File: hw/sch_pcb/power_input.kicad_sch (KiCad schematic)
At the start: 22 parts, among them J2 WAGO 256 RED, J3 WAGO 256 BLUE, J4 HEADER_2x01_PARALLEL, U3 SPV1040

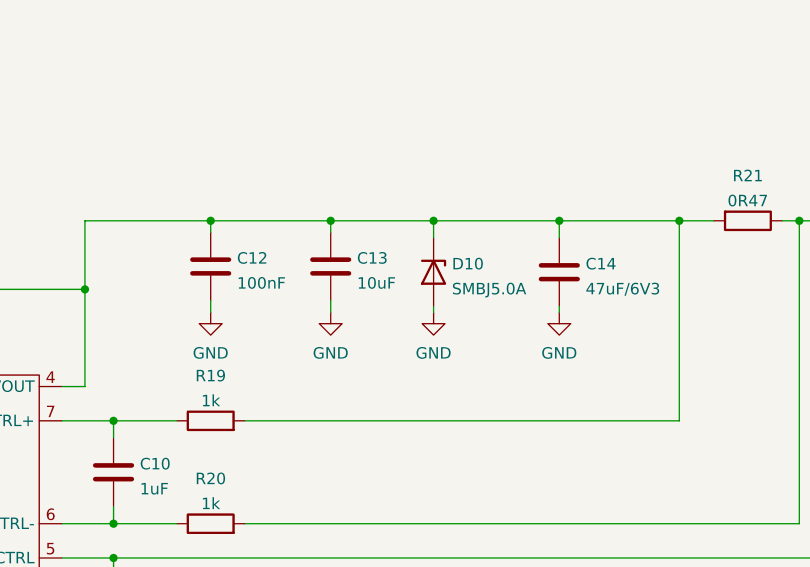
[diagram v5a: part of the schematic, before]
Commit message: Edit UST ID
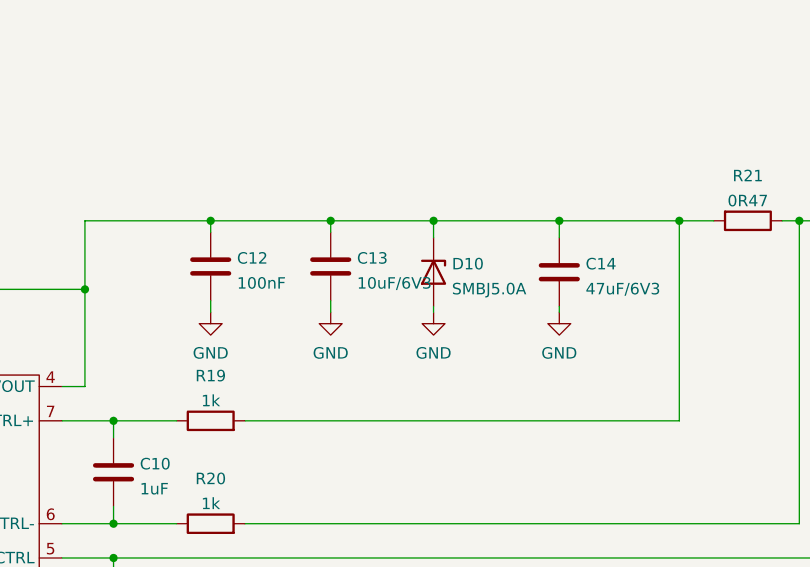
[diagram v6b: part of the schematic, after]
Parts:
- C10: UST_ID (none) -> 5c70984712875079b91f8b50
- C11: UST_ID (none) -> 5c70984712875079b91f8b45
- C12, C9: UST_ID (none) -> 5c70984712875079b91f8b4c
- C13: value 10uF -> 10uF/6V3; UST_ID (none) -> 5c70984712875079b91f8b53
- C14, C15, C8: UST_ID (none) -> 60d580ff1287500165f8595a
- D10: UST_ID (none) -> 5c70984512875079b91f88c7
- D9: UST_ID (none) -> 5c70984512875079b91f88b0
- J2: value WAGO 256 RED -> WAGO 256 ORANGE; UST_ID (none) -> 5c70984412875079b91f87c4
- J3: UST_ID (none) -> 5c70984412875079b91f87c3
- L1: UST_ID (none) -> 5c70984412875079b91f8822
- R17, R18, R19, R20: UST_ID (none) -> 5c70984512875079b91f898c
- R21: UST_ID (none) -> 60be2ed51287500165e6c1cd
- R22: UST_ID (none) -> 5c70984712875079b91f8aa6
- R23: UST_ID (none) -> 5c70984712875079b91f8aa0
- U3: UST_ID (none) -> 5c70984612875079b91f89bc
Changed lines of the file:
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@@
       (effects (font (size 1.27 1.27)) hide)
     )
-    (property "UST_ID" "" (id 4) (at 141.605 106.68 0)
+    (property "UST_ID" "5c70984712875079b91f8b45" (id 4) (at 141.605 106.68 0)
       (effects (font (size 1.27 1.27)) hide)
     )
@@
       (effects (font (size 1.27 1.27)) hide)
     )
-    (property "UST_ID" "" (id 4) (at 93.345 106.68 0)
+    (property "UST_ID" "5c70984712875079b91f8b4c" (id 4) (at 93.345 106.68 0)
       (effects (font (size 1.27 1.27)) hide)
     )
@@
       (effects (font (size 1.27 1.27)) hide)
     )
-    (property "UST_ID" "" (id 4) (at 152.4 68.58 0)
+    (property "UST_ID" "5c70984712875079b91f8b4c" (id 4) (at 152.4 68.58 0)
       (effects (font (size 1.27 1.27)) hide)
     )
@@
       (effects (font (size 1.27 1.27)) (justify left))
     )
-    (property "Value" "10uF" (id 1) (at 168.656 70.4466 0)
+    (property "Value" "10uF/6V3" (id 1) (at 168.656 70.4466 0)
       (effects (font (size 1.27 1.27)) (justify left))
     )
@@
       (effects (font (size 1.27 1.27)) hide)
     )
-    (property "UST_ID" "" (id 4) (at 165.735 68.58 0)
+    (property "UST_ID" "5c70984712875079b91f8b53" (id 4) (at 165.735 68.58 0)
       (effects (font (size 1.27 1.27)) hide)
     )
@@
       (effects (font (size 1.27 1.27)) hide)
     )
-    (property "UST_ID" "" (id 4) (at 222.885 105.41 0)
+    (property "UST_ID" "5c70984712875079b91f8aa0" (id 4) (at 222.885 105.41 0)
       (effects (font (size 1.27 1.27)) hide)
     )
@@
       (effects (font (size 1.27 1.27)) hide)
     )
-    (property "UST_ID" "" (id 4) (at 177.165 69.215 0)
+    (property "UST_ID" "5c70984512875079b91f88c7" (id 4) (at 177.165 69.215 0)
       (effects (font (size 1.27 1.27)) hide)
     )
@@
       (effects (font (size 1.27 1.27)) hide)
     )
-    (property "UST_ID" "" (id 4) (at 123.19 88.265 0)
+    (property "UST_ID" "5c70984612875079b91f89bc" (id 4) (at 123.19 88.265 0)
       (effects (font (size 1.27 1.27)) hide)
     )
@@
       (effects (font (size 1.27 1.27)) hide)
     )
+    (property "UST_ID" "60d580ff1287500165f8595a" (id 4) (at 191.135 69.215 0)
+      (effects (font (size 1.27 1.27)) hide)
+    )
     (pin "1")
     (pin "2")
@@
     )
     (property "Datasheet" "~" (id 3) (at 67.945 95.885 0)
+      (effects (font (size 1.27 1.27)) hide)
+    )
+    (property "UST_ID" "60d580ff1287500165f8595a" (id 4) (at 67.945 95.885 0)
       (effects (font (size 1.27 1.27)) hide)
     )
@@
       (effects (font (size 1.27 1.27)) hide)
     )
-    (property "UST_ID" "" (id 4) (at 122.555 71.12 0)
+    (property "UST_ID" "5c70984512875079b91f88b0" (id 4) (at 122.555 71.12 0)
       (effects (font (size 1.27 1.27)) hide)
     )
@@
       (effects (font (size 1.524 1.524)))
     )
-    (property "UST_ID" "" (id 4) (at 53.34 102.235 0)
+    (property "UST_ID" "5c70984412875079b91f87c3" (id 4) (at 53.34 102.235 0)
       (effects (font (size 1.27 1.27)) hide)
     )
@@
     (in_bom yes) (on_board yes)
     (property "Reference" "J2" (id 0) (at 52.705 81.915 0))
-    (property "Value" "WAGO 256 RED" (id 1) (at 50.8 79.375 0)
+    (property "Value" "WAGO 256 ORANGE" (id 1) (at 50.8 79.375 0)
       (effects (font (size 1.016 1.016)) hide)
     )
@@
       (effects (font (size 1.524 1.524)))
     )
-    (property "UST_ID" "" (id 4) (at 53.34 80.645 0)
+    (property "UST_ID" "5c70984412875079b91f87c4" (id 4) (at 53.34 80.645 0)
       (effects (font (size 1.27 1.27)) hide)
     )
@@
       (effects (font (size 1.27 1.27)) hide)
     )
-    (property "UST_ID" "" (id 4) (at 152.4 97.155 0)
+    (property "UST_ID" "5c70984512875079b91f898c" (id 4) (at 152.4 97.155 0)
       (effects (font (size 1.27 1.27)) hide)
     )
@@
       (effects (font (size 1.27 1.27)) hide)
     )
-    (property "UST_ID" "" (id 4) (at 82.55 94.615 0)
+    (property "UST_ID" "5c70984512875079b91f898c" (id 4) (at 82.55 94.615 0)
       (effects (font (size 1.27 1.27)) hide)
     )
@@
       (effects (font (size 1.27 1.27)) hide)
     )
-    (property "UST_ID" "" (id 4) (at 95.885 88.265 0)
+    (property "UST_ID" "5c70984512875079b91f898c" (id 4) (at 95.885 88.265 0)
       (effects (font (size 1.27 1.27)) hide)
     )
@@
     )
     (property "Datasheet" "~" (id 3) (at 229.87 69.215 0)
+      (effects (font (size 1.27 1.27)) hide)
+    )
+    (property "UST_ID" "60d580ff1287500165f8595a" (id 4) (at 229.87 69.215 0)
       (effects (font (size 1.27 1.27)) hide)
     )
@@
       (effects (font (size 1.27 1.27)) hide)
     )
-    (property "UST_ID" "" (id 4) (at 152.4 85.725 0)
+    (property "UST_ID" "5c70984512875079b91f898c" (id 4) (at 152.4 85.725 0)
       (effects (font (size 1.27 1.27)) hide)
     )
@@
       (effects (font (size 1.27 1.27)) hide)
     )
-    (property "UST_ID" "" (id 4) (at 212.09 63.5 0)
+    (property "UST_ID" "60be2ed51287500165e6c1cd" (id 4) (at 212.09 63.5 0)
       (effects (font (size 1.27 1.27)) hide)
     )
@@
       (effects (font (size 1.27 1.27)) hide)
     )
-    (property "UST_ID" "" (id 4) (at 141.605 91.44 0)
+    (property "UST_ID" "5c70984712875079b91f8b50" (id 4) (at 141.605 91.44 0)
       (effects (font (size 1.27 1.27)) hide)
     )
@@
       (effects (font (size 1.27 1.27)) hide)
     )
-    (property "UST_ID" "" (id 4) (at 222.885 93.345 0)
+    (property "UST_ID" "5c70984712875079b91f8aa6" (id 4) (at 222.885 93.345 0)
       (effects (font (size 1.27 1.27)) hide)
     )
@@
       (effects (font (size 1.27 1.27)) hide)
     )
-    (property "UST_ID" "" (id 4) (at 102.87 81.915 0)
-      (effects (font (size 1.27 1.27)) hide)
-    )
+    (property "UST_ID" "5c70984412875079b91f8822" (id 4) (at 102.87 81.915 0)
+      (effects (font (size 1.27 1.27)) hide)
+    )

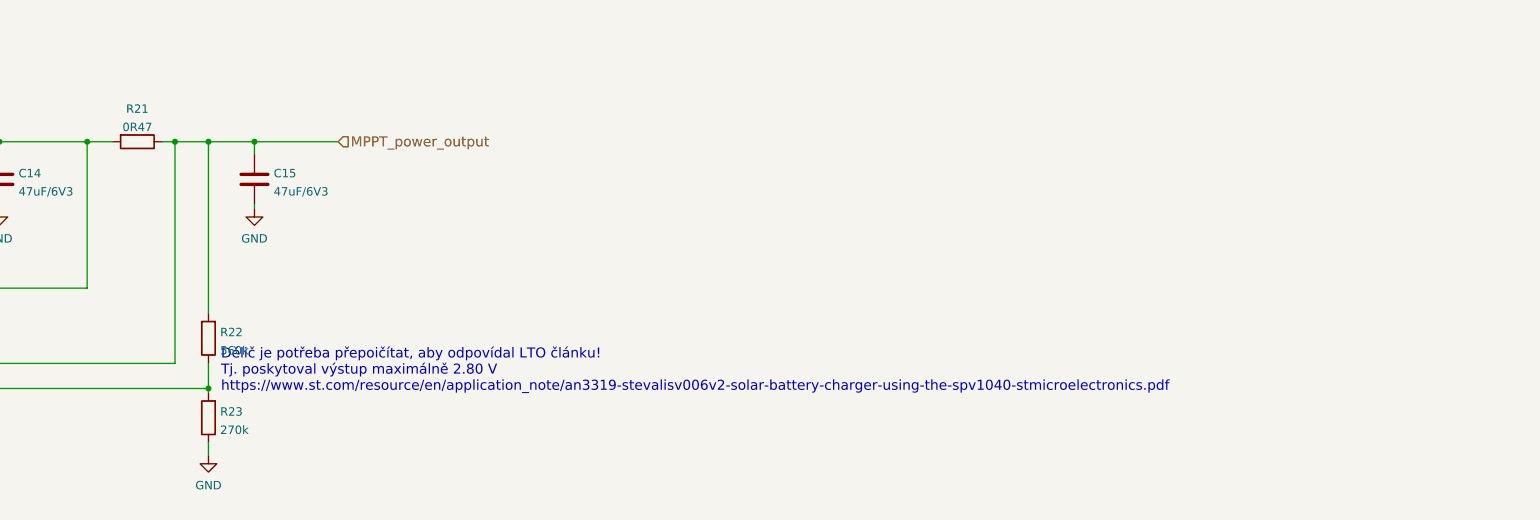
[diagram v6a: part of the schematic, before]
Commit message: Edit UST ID
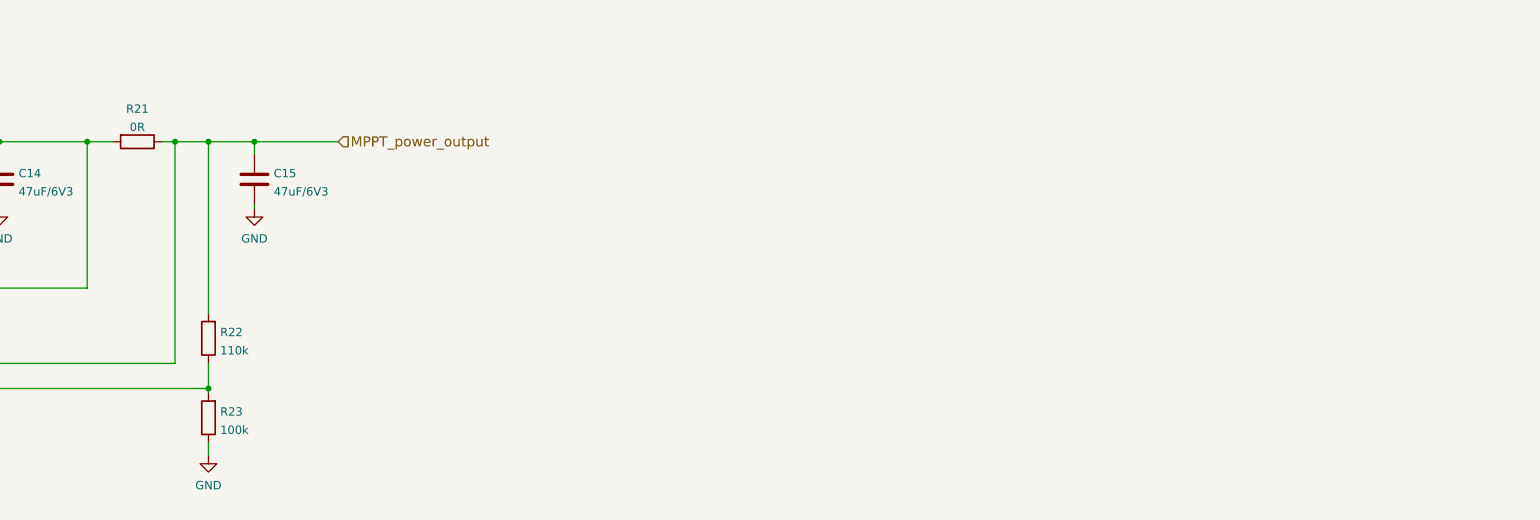
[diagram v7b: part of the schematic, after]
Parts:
- R21: value 0R47 -> 0R; UST_ID 60be2ed51287500165e6c1cd -> 5c70984712875079b91f8aaf
- R22: value 560k -> 110k; UST_ID 5c70984712875079b91f8aa6 -> 5e3ffc4a1287502a33bad850
- R23: value 270k -> 100k; UST_ID 5c70984712875079b91f8aa0 -> 5c70984712875079b91f8a96
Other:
- note removed: "Dělič je potřeba přepoičítat, aby odpovídal LTO článku! Tj. poskytoval výstup maximálně 2.80 V https://www.st.com/resource/en/application_note/an3319-stevalisv006v2-solar-battery-charger-using-the-spv1040-stmicroelectronics.pdf"
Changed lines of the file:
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@@
     (effects (font (size 1.27 1.27)) (justify left bottom))
-  )
-  (text "Dělič je potřeba přepoičítat, aby odpovídal LTO článku!\nTj. poskytoval výstup maximálně 2.80 V\nhttps://www.st.com/resource/en/application_note/an3319-stevalisv006v2-solar-battery-charger-using-the-spv1040-stmicroelectronics.pdf"
-    (at 224.79 101.6 0)
-    (effects (font (size 1.524 1.524)) (justify left bottom))
   )
   (text "Solar Cell Panel Connection" (at 111.125 29.845 0)
@@
       (effects (font (size 1.27 1.27)) (justify right))
     )
-    (property "Value" "270k" (id 1) (at 224.663 107.2766 0)
+    (property "Value" "100k" (id 1) (at 224.663 107.2766 0)
       (effects (font (size 1.27 1.27)) (justify right))
     )
@@
       (effects (font (size 1.27 1.27)) hide)
     )
-    (property "UST_ID" "5c70984712875079b91f8aa0" (id 4) (at 222.885 105.41 0)
+    (property "UST_ID" "5c70984712875079b91f8a96" (id 4) (at 222.885 105.41 0)
       (effects (font (size 1.27 1.27)) hide)
     )
@@
     (in_bom yes) (on_board yes) (fields_autoplaced)
     (property "Reference" "R21" (id 0) (at 212.09 58.5175 90))
-    (property "Value" "0R47" (id 1) (at 212.09 61.2926 90))
+    (property "Value" "0R" (id 1) (at 212.09 61.2926 90))
     (property "Footprint" "Resistor_SMD:R_1206_3216Metric" (id 2) (at 212.09 61.722 90)
       (effects (font (size 1.27 1.27)) hide)
@@
       (effects (font (size 1.27 1.27)) hide)
     )
-    (property "UST_ID" "60be2ed51287500165e6c1cd" (id 4) (at 212.09 63.5 0)
+    (property "UST_ID" "5c70984712875079b91f8aaf" (id 4) (at 212.09 63.5 0)
       (effects (font (size 1.27 1.27)) hide)
     )
@@
       (effects (font (size 1.27 1.27)) (justify right))
     )
-    (property "Value" "560k" (id 1) (at 224.663 95.2116 0)
+    (property "Value" "110k" (id 1) (at 224.663 95.2116 0)
       (effects (font (size 1.27 1.27)) (justify right))
     )
@@
       (effects (font (size 1.27 1.27)) hide)
     )
-    (property "UST_ID" "5c70984712875079b91f8aa6" (id 4) (at 222.885 93.345 0)
-      (effects (font (size 1.27 1.27)) hide)
-    )
+    (property "UST_ID" "5e3ffc4a1287502a33bad850" (id 4) (at 222.885 93.345 0)
+      (effects (font (size 1.27 1.27)) hide)
+    )
